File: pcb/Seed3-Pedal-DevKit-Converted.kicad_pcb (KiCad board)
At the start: 2 copper layers, 197 x 100 mm, 166 parts, among them J1 DIN_MIDI_5P, J10 DIN_MIDI_5P, J11 DIN_MIDI_5P, J2 JACK_TRS_SWITCHING, J3 JACK_TRS_SWITCHING, J4 JACK_TRS_SWITCHING, J5 JACK_TRS_SWITCHING, J6 JACK_TRS_SWITCHING, J8 Barrel_Jack_Switch, Q1 3904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

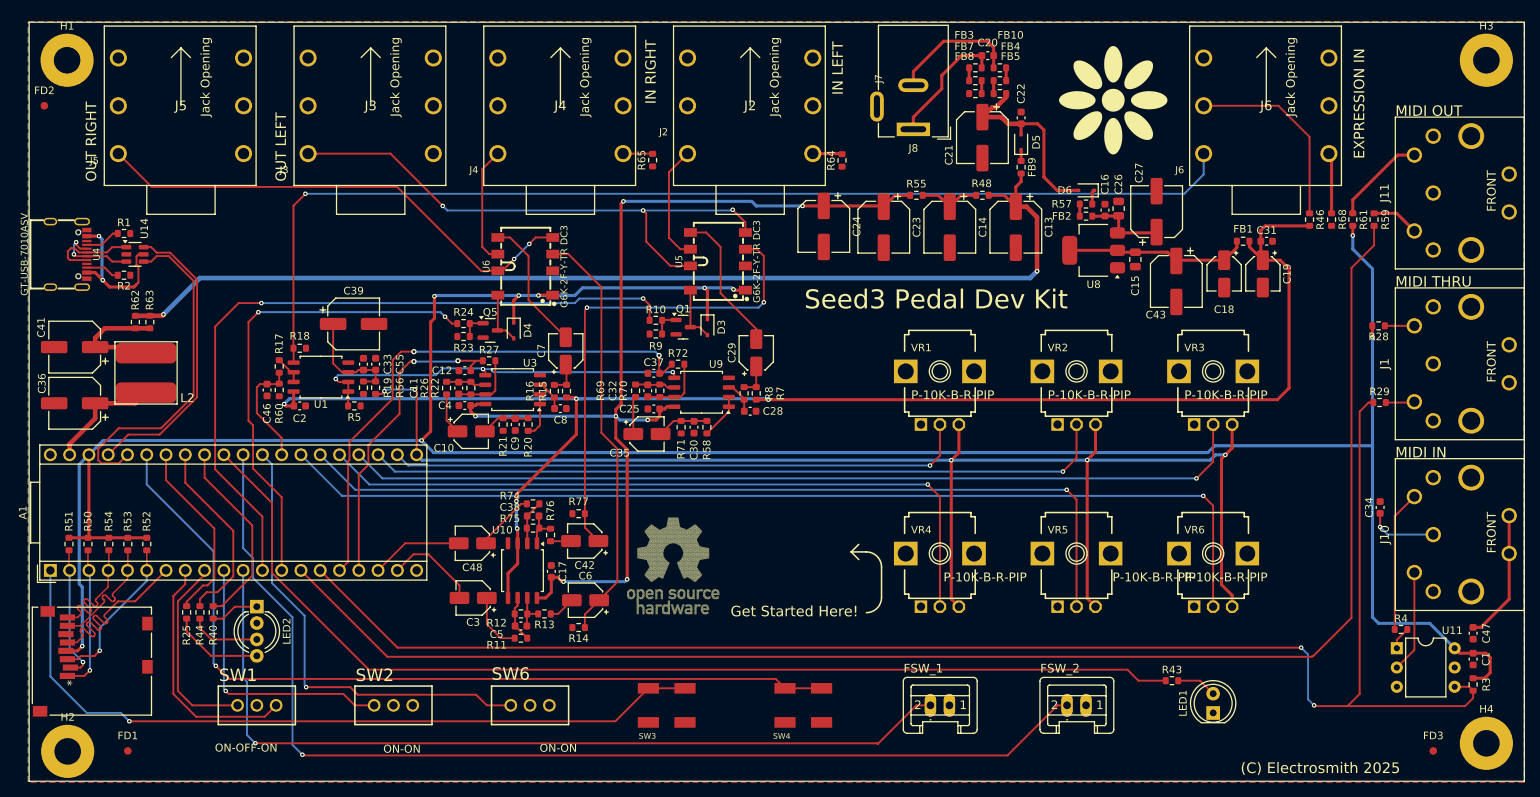
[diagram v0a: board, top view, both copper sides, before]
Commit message: everything except for rounding corners and renaming
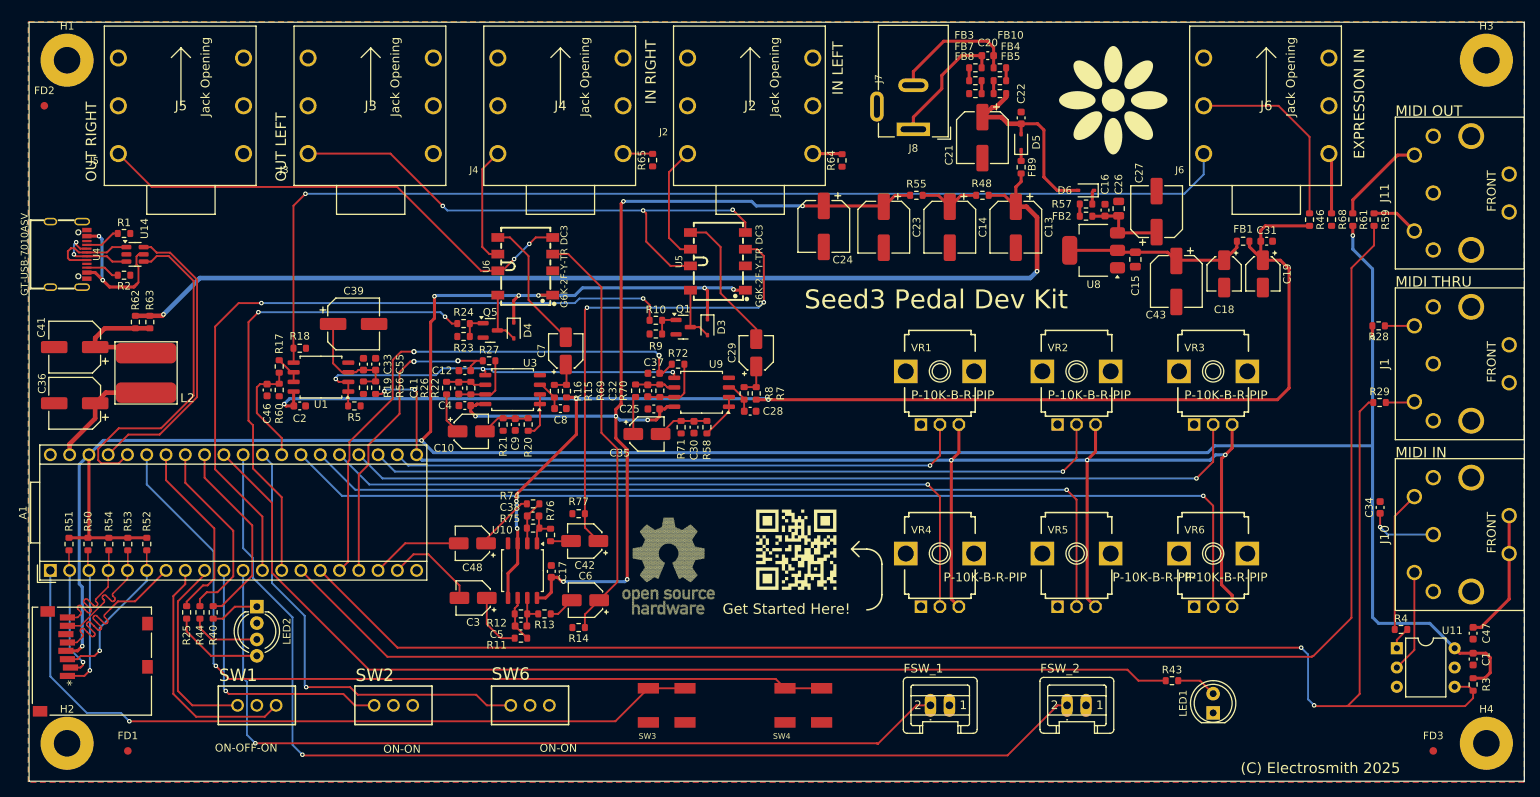
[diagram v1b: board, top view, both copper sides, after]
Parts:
- moved H2 1.07 mm to (55.0, 150.0)
- moved LOGO1 0.61 mm to (134.2, 127.9)
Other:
- board text added: "Black"
- board text added: "ENIG"
- board text added: "Rev1"
- board text added: "White"
- board text removed: "None"
